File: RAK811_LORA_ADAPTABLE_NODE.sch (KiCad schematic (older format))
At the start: 6 parts

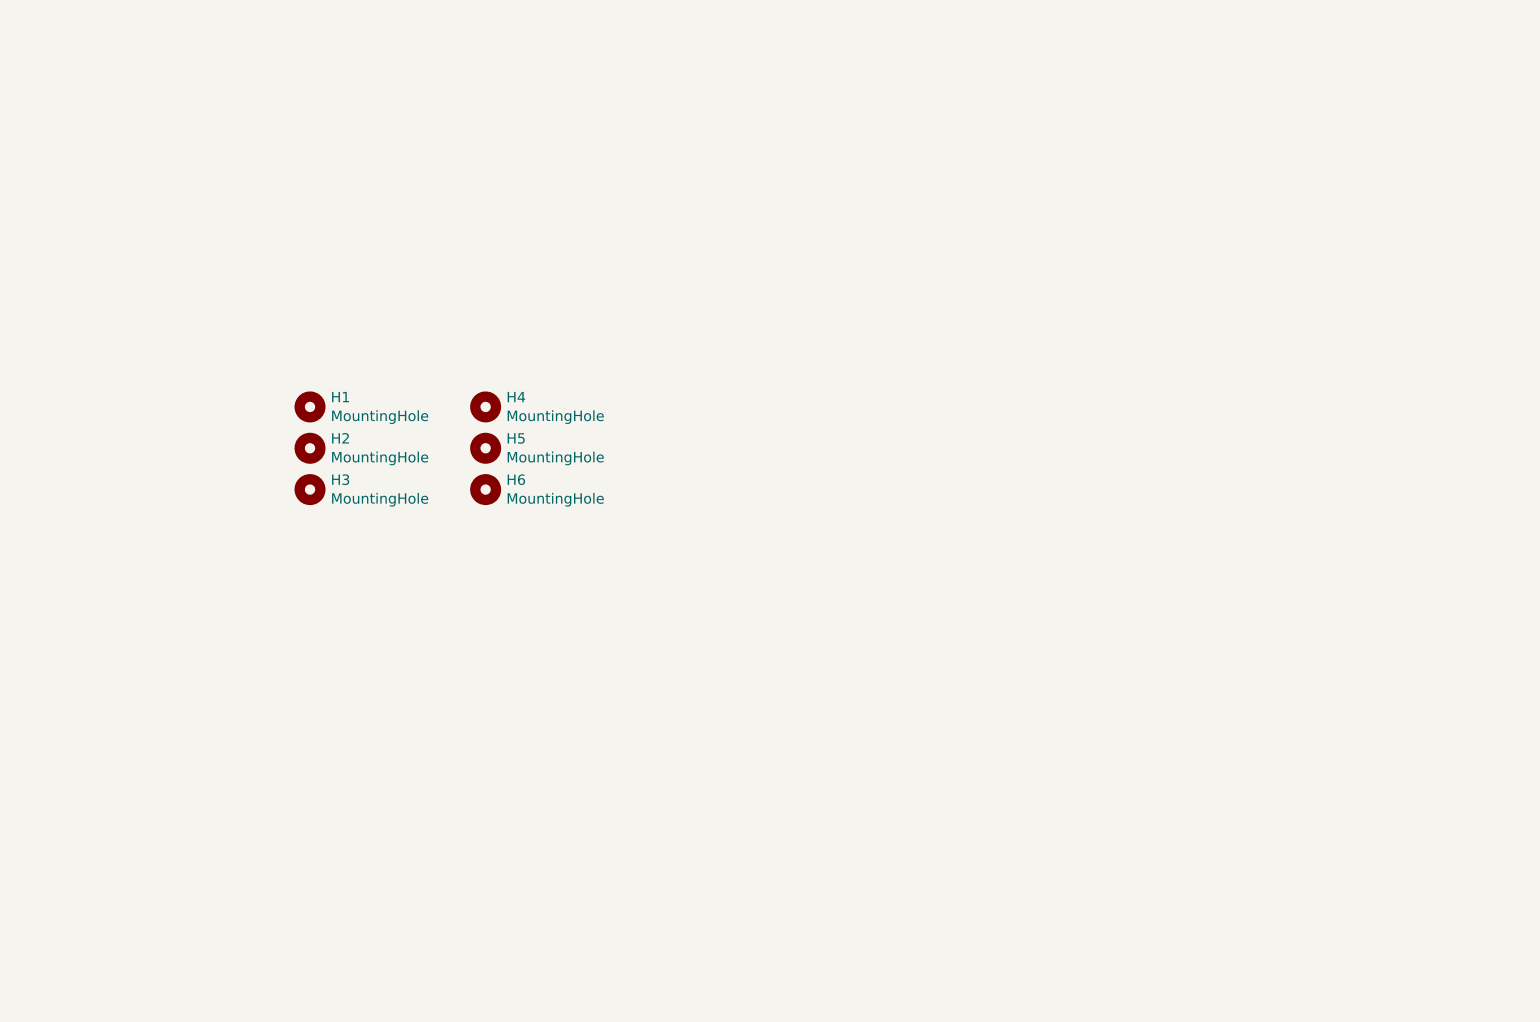
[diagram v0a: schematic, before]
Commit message: put basic elements: lora mudule, battery holders, screw connectors
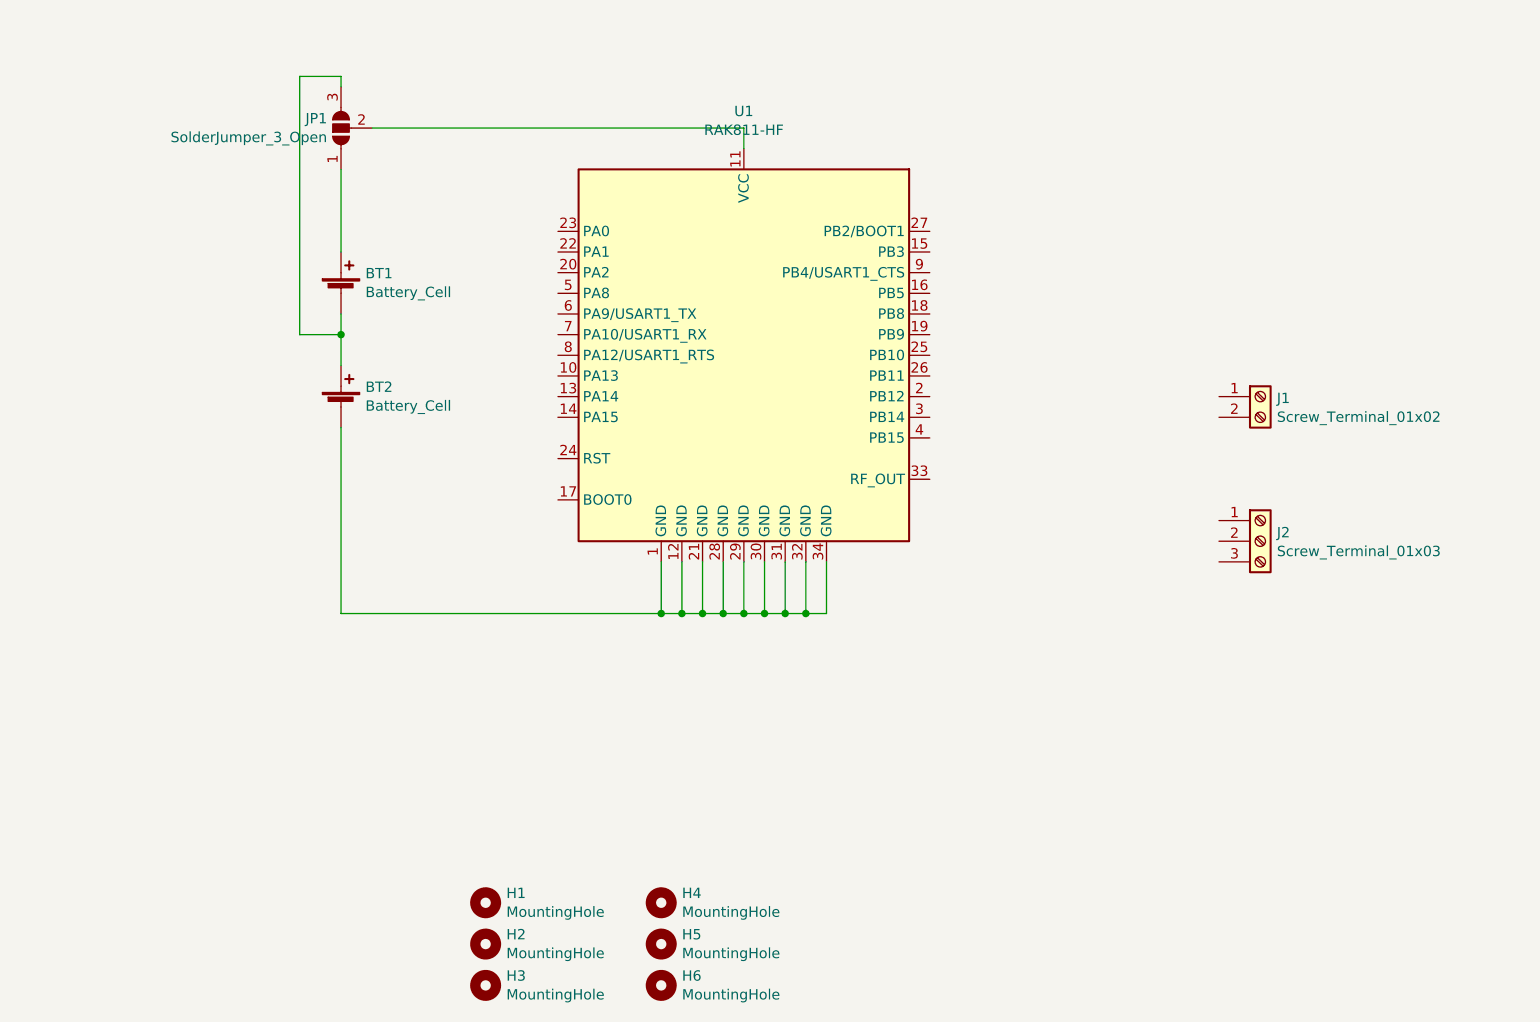
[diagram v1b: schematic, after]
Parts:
- added BT1, BT2: Battery_Cell, Battery:BatteryHolder_Keystone_2460_1xAA, symbol Device:Battery_Cell
- added J1: Screw_Terminal_01x02, TerminalBlock_4Ucon:TerminalBlock_4Ucon_1x02_P3.50mm_Horizontal, symbol Connector:Screw_Terminal_01x02
- added J2: Screw_Terminal_01x03, TerminalBlock_4Ucon:TerminalBlock_4Ucon_1x03_P3.50mm_Horizontal, symbol Connector:Screw_Terminal_01x03
- added JP1: SolderJumper_3_Open, Jumper:SolderJumper-3_P1.3mm_Open_RoundedPad1.0x1.5mm_NumberLabels, symbol Jumper:SolderJumper_3_Open
- added U1: RAK811-HF, RF_Module:RAK811, symbol RF_Module:RAK811-HF
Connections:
- new net: BT2.2 (-), U1.1 (GND), U1.12 (GND), U1.21 (GND), U1.28 (GND), U1.29 (GND), U1.30 (GND), U1.31 (GND), U1.32 (GND), U1.34 (GND)
- new net: JP1.2 (C), U1.11 (VCC)
- new net: BT1.1 (+), JP1.1 (A)
- new net: BT1.2 (-), BT2.1 (+), JP1.3 (B)
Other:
- moved on the sheet: H1, H2, H3, H4, H5, H6
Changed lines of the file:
@@
 L Mechanical:MountingHole H1
 U 1 1 5EED2AEB
-P 3350 3200
-F 0 "H1" H 3450 3246 50  0000 L CNN
-F 1 "MountingHole" H 3450 3155 50  0000 L CNN
-F 2 "MountingHole:MountingHole_3mm" H 3350 3200 50  0001 C CNN
-F 3 "~" H 3350 3200 50  0001 C CNN
-	1    3350 3200
+P 4200 5600
+F 0 "H1" H 4300 5646 50  0000 L CNN
+F 1 "MountingHole" H 4300 5555 50  0000 L CNN
+F 2 "MountingHole:MountingHole_3mm" H 4200 5600 50  0001 C CNN
+F 3 "~" H 4200 5600 50  0001 C CNN
+	1    4200 5600
 	1    0    0    -1
 $EndComp
@@
 L Mechanical:MountingHole H2
 U 1 1 5EED2E39
-P 3350 3400
-F 0 "H2" H 3450 3446 50  0000 L CNN
-F 1 "MountingHole" H 3450 3355 50  0000 L CNN
-F 2 "MountingHole:MountingHole_3mm" H 3350 3400 50  0001 C CNN
-F 3 "~" H 3350 3400 50  0001 C CNN
-	1    3350 3400
+P 4200 5800
+F 0 "H2" H 4300 5846 50  0000 L CNN
+F 1 "MountingHole" H 4300 5755 50  0000 L CNN
+F 2 "MountingHole:MountingHole_3mm" H 4200 5800 50  0001 C CNN
+F 3 "~" H 4200 5800 50  0001 C CNN
+	1    4200 5800
 	1    0    0    -1
 $EndComp
@@
 L Mechanical:MountingHole H3
 U 1 1 5EED3144
-P 3350 3600
-F 0 "H3" H 3450 3646 50  0000 L CNN
-F 1 "MountingHole" H 3450 3555 50  0000 L CNN
-F 2 "MountingHole:MountingHole_3mm" H 3350 3600 50  0001 C CNN
-F 3 "~" H 3350 3600 50  0001 C CNN
-	1    3350 3600
+P 4200 6000
+F 0 "H3" H 4300 6046 50  0000 L CNN
+F 1 "MountingHole" H 4300 5955 50  0000 L CNN
+F 2 "MountingHole:MountingHole_3mm" H 4200 6000 50  0001 C CNN
+F 3 "~" H 4200 6000 50  0001 C CNN
+	1    4200 6000
 	1    0    0    -1
 $EndComp
@@
 L Mechanical:MountingHole H4
 U 1 1 5EED33AC
-P 4200 3200
-F 0 "H4" H 4300 3246 50  0000 L CNN
-F 1 "MountingHole" H 4300 3155 50  0000 L CNN
-F 2 "MountingHole:MountingHole_3mm" H 4200 3200 50  0001 C CNN
-F 3 "~" H 4200 3200 50  0001 C CNN
-	1    4200 3200
+P 5050 5600
+F 0 "H4" H 5150 5646 50  0000 L CNN
+F 1 "MountingHole" H 5150 5555 50  0000 L CNN
+F 2 "MountingHole:MountingHole_3mm" H 5050 5600 50  0001 C CNN
+F 3 "~" H 5050 5600 50  0001 C CNN
+	1    5050 5600
 	1    0    0    -1
 $EndComp
@@
 L Mechanical:MountingHole H6
 U 1 1 5EED36FB
-P 4200 3600
-F 0 "H6" H 4300 3646 50  0000 L CNN
-F 1 "MountingHole" H 4300 3555 50  0000 L CNN
-F 2 "MountingHole:MountingHole_3mm" H 4200 3600 50  0001 C CNN
-F 3 "~" H 4200 3600 50  0001 C CNN
-	1    4200 3600
+P 5050 6000
+F 0 "H6" H 5150 6046 50  0000 L CNN
+F 1 "MountingHole" H 5150 5955 50  0000 L CNN
+F 2 "MountingHole:MountingHole_3mm" H 5050 6000 50  0001 C CNN
+F 3 "~" H 5050 6000 50  0001 C CNN
+	1    5050 6000
 	1    0    0    -1
 $EndComp
@@
 L Mechanical:MountingHole H5
 U 1 1 5EED3A44
-P 4200 3400
-F 0 "H5" H 4300 3446 50  0000 L CNN
-F 1 "MountingHole" H 4300 3355 50  0000 L CNN
-F 2 "MountingHole:MountingHole_3mm" H 4200 3400 50  0001 C CNN
-F 3 "~" H 4200 3400 50  0001 C CNN
-	1    4200 3400
+P 5050 5800
+F 0 "H5" H 5150 5846 50  0000 L CNN
+F 1 "MountingHole" H 5150 5755 50  0000 L CNN
+F 2 "MountingHole:MountingHole_3mm" H 5050 5800 50  0001 C CNN
+F 3 "~" H 5050 5800 50  0001 C CNN
+	1    5050 5800
 	1    0    0    -1
 $EndComp
+$Comp
+L RF_Module:RAK811-HF U1
+U 1 1 5EF19EE7
+P 5450 2950
+F 0 "U1" H 5450 4131 50  0000 C CNN
+F 1 "RAK811-HF" H 5450 4040 50  0000 C CNN
+F 2 "RF_Module:RAK811" H 5000 4200 50  0001 C CNN
+F 3 "https://downloads.rakwireless.com/LoRa/RAK811/Hardware_Specification/RAK811_LoRa_Module_Datasheet_V1.4.pdf" H 5000 4200 50  0001 C CNN
+	1    5450 2950
+	1    0    0    -1
+$EndComp
+$Comp
+L Device:Battery_Cell BT1
+U 1 1 5EF1CAC1
+P 3500 2650
+F 0 "BT1" H 3618 2746 50  0000 L CNN
+F 1 "Battery_Cell" H 3618 2655 50  0000 L CNN
+F 2 "Battery:BatteryHolder_Keystone_2460_1xAA" V 3500 2710 50  0001 C CNN
+F 3 "~" V 3500 2710 50  0001 C CNN
+	1    3500 2650
+	1    0    0    -1
+$EndComp
+$Comp
+L Device:Battery_Cell BT2
+U 1 1 5EF1E49F
+P 3500 3200
+F 0 "BT2" H 3618 3296 50  0000 L CNN
+F 1 "Battery_Cell" H 3618 3205 50  0000 L CNN
+F 2 "Battery:BatteryHolder_Keystone_2460_1xAA" V 3500 3260 50  0001 C CNN
+F 3 "~" V 3500 3260 50  0001 C CNN
+	1    3500 3200
+	1    0    0    -1
+$EndComp
+Wire Wire Line
+	5850 3950 5850 4200
+Wire Wire Line
+	5850 4200 5750 4200
+Wire Wire Line
+	3500 4200 3500 3300
+Wire Wire Line
+	5750 3950 5750 4200
+Connection ~ 5750 4200
+Wire Wire Line
+	5750 4200 5650 4200
+Wire Wire Line
+	5650 3950 5650 4200
+Connection ~ 5650 4200
+Wire Wire Line
+	5650 4200 5550 4200
+Wire Wire Line
+	5550 3950 5550 4200
+Connection ~ 5550 4200
+Wire Wire Line
+	5550 4200 5450 4200
+Wire Wire Line
+	5450 3950 5450 4200
+Connection ~ 5450 4200
+Wire Wire Line
+	5450 4200 5350 4200
+Wire Wire Line
+	5350 3950 5350 4200
+Connection ~ 5350 4200
+Wire Wire Line
+	5350 4200 5250 4200
+Wire Wire Line
+	5250 3950 5250 4200
+Connection ~ 5250 4200
+Wire Wire Line
+	5250 4200 5150 4200
+Wire Wire Line
+	5150 3950 5150 4200
+Connection ~ 5150 4200
+Wire Wire Line
+	5150 4200 5050 4200
+Wire Wire Line
+	5050 3950 5050 4200
+Connection ~ 5050 4200
+Wire Wire Line
+	5050 4200 3500 4200
+$Comp
+L Jumper:SolderJumper_3_Open JP1
+U 1 1 5EF24551
+P 3500 1850
+F 0 "JP1" V 3546 1917 50  0000 L CNN
+F 1 "SolderJumper_3_Open" V 3455 1917 50  0000 L CNN
+F 2 "Jumper:SolderJumper-3_P1.3mm_Open_RoundedPad1.0x1.5mm_NumberLabels" H 3500 1850 50  0001 C CNN
+F 3 "~" H 3500 1850 50  0001 C CNN
+	1    3500 1850
+	0    -1   -1   0
+$EndComp
+Wire Wire Line
+	3650 1850 5450 1850
+Wire Wire Line
+	5450 1850 5450 1950
+Wire Wire Line
+	3500 2050 3500 2450
+Wire Wire Line
+	3500 3000 3500 2850
+Wire Wire Line
+	3500 2850 3300 2850
+Wire Wire Line
+	3300 2850 3300 1600
+Wire Wire Line
+	3300 1600 3500 1600
+Wire Wire Line
+	3500 1600 3500 1650
+Connection ~ 3500 2850
+Wire Wire Line
+	3500 2850 3500 2750
+$Comp
+L Connector:Screw_Terminal_01x02 J1
+U 1 1 5EF232A0
+P 7950 3150
+F 0 "J1" H 8030 3142 50  0000 L CNN
+F 1 "Screw_Terminal_01x02" H 8030 3051 50  0000 L CNN
+F 2 "TerminalBlock_4Ucon:TerminalBlock_4Ucon_1x02_P3.50mm_Horizontal" H 7950 3150 50  0001 C CNN
+F 3 "~" H 7950 3150 50  0001 C CNN
+	1    7950 3150
+	1    0    0    -1
+$EndComp
+$Comp
+L Connector:Screw_Terminal_01x03 J2
+U 1 1 5EF238D6
+P 7950 3850
+F 0 "J2" H 8030 3892 50  0000 L CNN
+F 1 "Screw_Terminal_01x03" H 8030 3801 50  0000 L CNN
+F 2 "TerminalBlock_4Ucon:TerminalBlock_4Ucon_1x03_P3.50mm_Horizontal" H 7950 3850 50  0001 C CNN
+F 3 "~" H 7950 3850 50  0001 C CNN
+	1    7950 3850
+	1    0    0    -1
+$EndComp

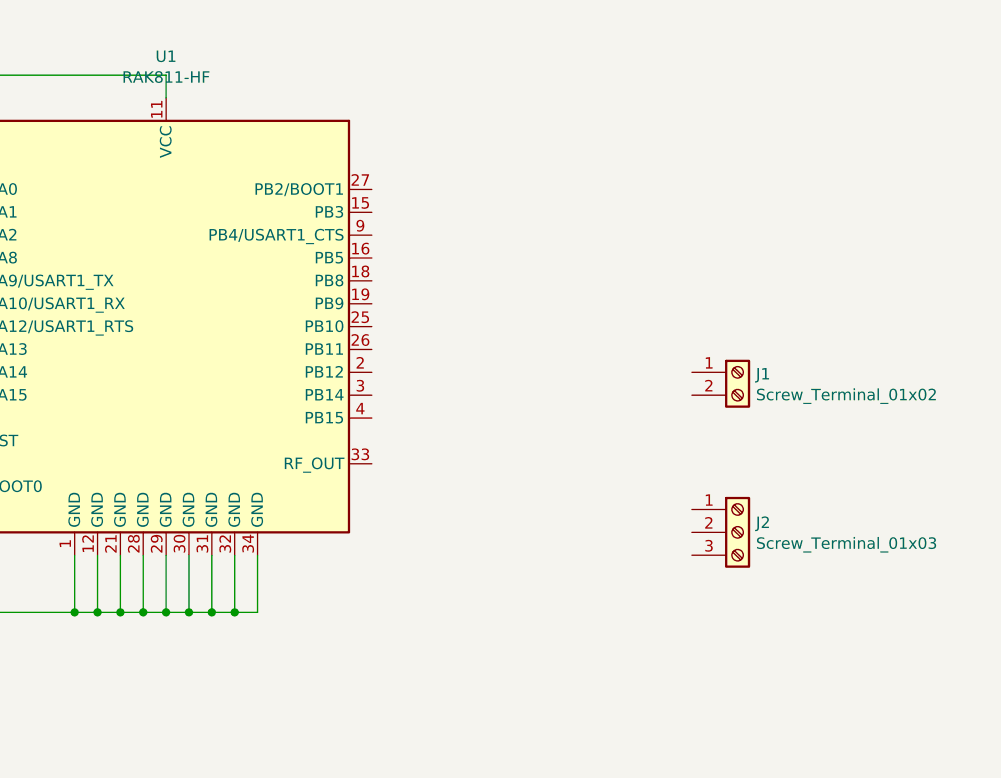
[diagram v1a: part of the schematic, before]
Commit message: add antenna output connectors
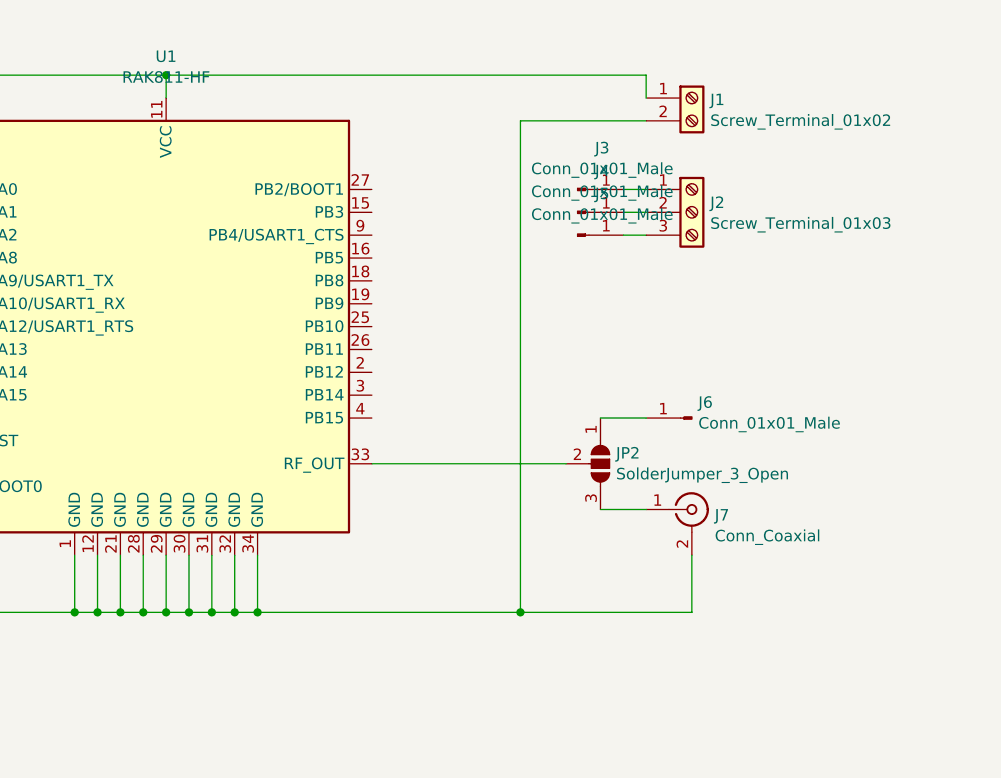
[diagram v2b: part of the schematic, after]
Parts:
- added J3, J4, J5, J6: Conn_01x01_Male, Connector_Wire:SolderWirePad_1x01_Drill0.8mm, symbol Connector:Conn_01x01_Male
- added J7: Conn_Coaxial, Connector_Coaxial:U.FL_Hirose_U.FL-R-SMT-1_Vertical, symbol Connector:Conn_Coaxial
- added JP2: SolderJumper_3_Open, Jumper:SolderJumper-3_P1.3mm_Open_RoundedPad1.0x1.5mm_NumberLabels, symbol Jumper:SolderJumper_3_Open
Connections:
- net at BT2.2 (-), U1.1 (GND), U1.12 (GND)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: now also J1.2 (Pin_2), J7.2 (Ext)
- net at JP1.2 (C), U1.11 (VCC): now also J1.1 (Pin_1)
- net at U1.33 (RF_OUT): now also JP2.2 (C)
- net at J2.1 (Pin_1): now also J3.1 (Pin_1)
- net at J2.2 (Pin_2): now also J4.1 (Pin_1)
- net at J2.3 (Pin_3): now also J5.1 (Pin_1)
- new net: J7.1 (In), JP2.3 (B)
- new net: J6.1 (Pin_1), JP2.1 (A)
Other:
- moved on the sheet: J1, J2
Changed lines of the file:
@@
 L Connector:Screw_Terminal_01x02 J1
 U 1 1 5EF232A0
-P 7950 3150
-F 0 "J1" H 8030 3142 50  0000 L CNN
-F 1 "Screw_Terminal_01x02" H 8030 3051 50  0000 L CNN
-F 2 "TerminalBlock_4Ucon:TerminalBlock_4Ucon_1x02_P3.50mm_Horizontal" H 7950 3150 50  0001 C CNN
-F 3 "~" H 7950 3150 50  0001 C CNN
-	1    7950 3150
+P 7750 1950
+F 0 "J1" H 7830 1942 50  0000 L CNN
+F 1 "Screw_Terminal_01x02" H 7830 1851 50  0000 L CNN
+F 2 "TerminalBlock_4Ucon:TerminalBlock_4Ucon_1x02_P3.50mm_Horizontal" H 7750 1950 50  0001 C CNN
+F 3 "~" H 7750 1950 50  0001 C CNN
+	1    7750 1950
 	1    0    0    -1
 $EndComp
@@
 L Connector:Screw_Terminal_01x03 J2
 U 1 1 5EF238D6
-P 7950 3850
-F 0 "J2" H 8030 3892 50  0000 L CNN
-F 1 "Screw_Terminal_01x03" H 8030 3801 50  0000 L CNN
-F 2 "TerminalBlock_4Ucon:TerminalBlock_4Ucon_1x03_P3.50mm_Horizontal" H 7950 3850 50  0001 C CNN
-F 3 "~" H 7950 3850 50  0001 C CNN
-	1    7950 3850
+P 7750 2450
+F 0 "J2" H 7830 2492 50  0000 L CNN
+F 1 "Screw_Terminal_01x03" H 7830 2401 50  0000 L CNN
+F 2 "TerminalBlock_4Ucon:TerminalBlock_4Ucon_1x03_P3.50mm_Horizontal" H 7750 2450 50  0001 C CNN
+F 3 "~" H 7750 2450 50  0001 C CNN
+	1    7750 2450
 	1    0    0    -1
 $EndComp
+Wire Wire Line
+	7550 1950 7550 1850
+Wire Wire Line
+	7550 1850 5450 1850
+Connection ~ 5450 1850
+Wire Wire Line
+	7550 2050 7000 2050
+Wire Wire Line
+	7000 2050 7000 4200
+Wire Wire Line
+	7000 4200 5850 4200
+Connection ~ 5850 4200
+$Comp
+L Connector:Conn_01x01_Male J3
+U 1 1 5EF3801E
+P 7250 2350
+F 0 "J3" H 7358 2531 50  0000 C CNN
+F 1 "Conn_01x01_Male" H 7358 2440 50  0000 C CNN
+F 2 "Connector_Wire:SolderWirePad_1x01_Drill0.8mm" H 7250 2350 50  0001 C CNN
+F 3 "~" H 7250 2350 50  0001 C CNN
+	1    7250 2350
+	1    0    0    -1
+$EndComp
+$Comp
+L Connector:Conn_01x01_Male J4
+U 1 1 5EF398BE
+P 7250 2450
+F 0 "J4" H 7358 2631 50  0000 C CNN
+F 1 "Conn_01x01_Male" H 7358 2540 50  0000 C CNN
+F 2 "Connector_Wire:SolderWirePad_1x01_Drill0.8mm" H 7250 2450 50  0001 C CNN
+F 3 "~" H 7250 2450 50  0001 C CNN
+	1    7250 2450
+	1    0    0    -1
+$EndComp
+$Comp
+L Connector:Conn_01x01_Male J5
+U 1 1 5EF39FD1
+P 7250 2550
+F 0 "J5" H 7358 2731 50  0000 C CNN
+F 1 "Conn_01x01_Male" H 7358 2640 50  0000 C CNN
+F 2 "Connector_Wire:SolderWirePad_1x01_Drill0.8mm" H 7250 2550 50  0001 C CNN
+F 3 "~" H 7250 2550 50  0001 C CNN
+	1    7250 2550
+	1    0    0    -1
+$EndComp
+Wire Wire Line
+	7450 2550 7550 2550
+Wire Wire Line
+	7450 2450 7550 2450
+Wire Wire Line
+	7450 2350 7550 2350
+$Comp
+L Connector:Conn_Coaxial J7
+U 1 1 5EF5A51C
+P 7750 3750
+F 0 "J7" H 7850 3725 50  0000 L CNN
+F 1 "Conn_Coaxial" H 7850 3634 50  0000 L CNN
+F 2 "Connector_Coaxial:U.FL_Hirose_U.FL-R-SMT-1_Vertical" H 7750 3750 50  0001 C CNN
+F 3 " ~" H 7750 3750 50  0001 C CNN
+	1    7750 3750
+	1    0    0    -1
+$EndComp
+$Comp
+L Jumper:SolderJumper_3_Open JP2
+U 1 1 5EF5B11F
+P 7350 3550
+F 0 "JP2" V 7304 3618 50  0000 L CNN
+F 1 "SolderJumper_3_Open" V 7395 3618 50  0000 L CNN
+F 2 "Jumper:SolderJumper-3_P1.3mm_Open_RoundedPad1.0x1.5mm_NumberLabels" H 7350 3550 50  0001 C CNN
+F 3 "~" H 7350 3550 50  0001 C CNN
+	1    7350 3550
+	0    1    1    0
+$EndComp
+$Comp
+L Connector:Conn_01x01_Male J6
+U 1 1 5EF704AE
+P 7750 3350
+F 0 "J6" H 7722 3282 50  0000 R CNN
+F 1 "Conn_01x01_Male" H 7722 3373 50  0000 R CNN
+F 2 "Connector_Wire:SolderWirePad_1x01_Drill0.8mm" H 7750 3350 50  0001 C CNN
+F 3 "~" H 7750 3350 50  0001 C CNN
+	1    7750 3350
+	-1   0    0    1
+$EndComp
+Wire Wire Line
+	6350 3550 7200 3550
+Wire Wire Line
+	7550 3350 7350 3350
+Wire Wire Line
+	7550 3750 7350 3750
+Wire Wire Line
+	7750 3950 7750 4200
+Wire Wire Line
+	7750 4200 7000 4200
+Connection ~ 7000 4200
 $EndSCHEMATC
